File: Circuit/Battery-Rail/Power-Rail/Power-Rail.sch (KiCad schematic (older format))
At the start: 4 parts, among them P1 XT60, P2 XT60, P3 XT60, P4 XT60

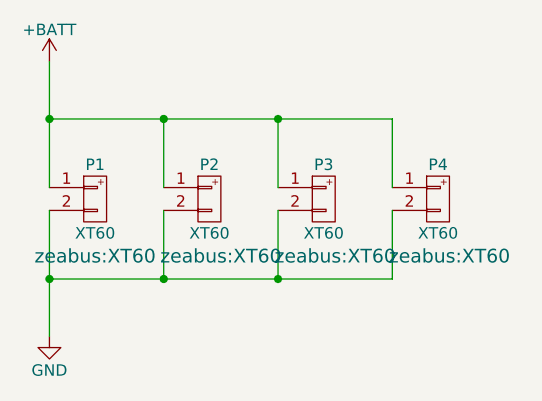
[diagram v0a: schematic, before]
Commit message: fix xt60 to close to each one on power-rail pcb
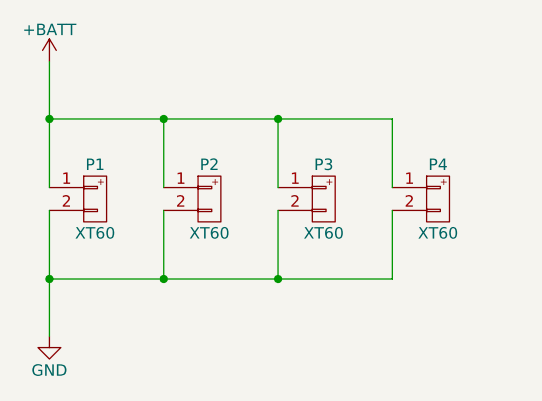
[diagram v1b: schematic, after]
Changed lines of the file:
@@
 LIBS:valves
 LIBS:zeabus
+LIBS:Power-Rail-cache
 EELAYER 25 0
 EELAYER END
@@
 Comment4 ""
 $EndDescr
-$Comp
-L XT60 P1
-U 1 1 594D2F0E
-P 5550 3850
-F 0 "P1" H 5550 4000 50  0000 C CNN
-F 1 "XT60" H 5550 3700 50  0000 C CNN
-F 2 "zeabus:XT60" H 5550 3600 60  0000 C CNN
-F 3 "" H 5550 3850 60  0000 C CNN
-	1    5550 3850
-	1    0    0    -1
-$EndComp
-$Comp
-L XT60 P2
-U 1 1 594D2F3F
-P 6050 3850
-F 0 "P2" H 6050 4000 50  0000 C CNN
-F 1 "XT60" H 6050 3700 50  0000 C CNN
-F 2 "zeabus:XT60" H 6100 3600 60  0000 C CNN
-F 3 "" H 6050 3850 60  0000 C CNN
-	1    6050 3850
-	1    0    0    -1
-$EndComp
-$Comp
-L XT60 P3
-U 1 1 594D30B5
-P 6550 3850
-F 0 "P3" H 6550 4000 50  0000 C CNN
-F 1 "XT60" H 6550 3700 50  0000 C CNN
-F 2 "zeabus:XT60" H 6600 3600 60  0000 C CNN
-F 3 "" H 6550 3850 60  0000 C CNN
-	1    6550 3850
-	1    0    0    -1
-$EndComp
-$Comp
-L XT60 P4
-U 1 1 594D30BB
-P 7050 3850
-F 0 "P4" H 7050 4000 50  0000 C CNN
-F 1 "XT60" H 7050 3700 50  0000 C CNN
-F 2 "zeabus:XT60" H 7100 3600 60  0000 C CNN
-F 3 "" H 7050 3850 60  0000 C CNN
-	1    7050 3850
-	1    0    0    -1
-$EndComp
 $Comp
 L +BATT #PWR01
@@
 	6850 4200 6850 3900
 Connection ~ 6350 4200
+$Comp
+L XT60 P1
+U 1 1 5A75305B
+P 5550 3850
+F 0 "P1" H 5550 4000 50  0000 C CNN
+F 1 "XT60" H 5550 3700 50  0000 C CNN
+F 2 "zeabus:XT60" H 5550 3850 60  0001 C CNN
+F 3 "" H 5550 3850 60  0000 C CNN
+	1    5550 3850
+	1    0    0    -1
+$EndComp
+$Comp
+L XT60 P2
+U 1 1 5A7531B6
+P 6050 3850
+F 0 "P2" H 6050 4000 50  0000 C CNN
+F 1 "XT60" H 6050 3700 50  0000 C CNN
+F 2 "zeabus:XT60" H 6050 3850 60  0001 C CNN
+F 3 "" H 6050 3850 60  0000 C CNN
+	1    6050 3850
+	1    0    0    -1
+$EndComp
+$Comp
+L XT60 P3
+U 1 1 5A7531DC
+P 6550 3850
+F 0 "P3" H 6550 4000 50  0000 C CNN
+F 1 "XT60" H 6550 3700 50  0000 C CNN
+F 2 "zeabus:XT60" H 6550 3850 60  0001 C CNN
+F 3 "" H 6550 3850 60  0000 C CNN
+	1    6550 3850
+	1    0    0    -1
+$EndComp
+$Comp
+L XT60 P4
+U 1 1 5A75320F
+P 7050 3850
+F 0 "P4" H 7050 4000 50  0000 C CNN
+F 1 "XT60" H 7050 3700 50  0000 C CNN
+F 2 "zeabus:XT60" H 7050 3850 60  0001 C CNN
+F 3 "" H 7050 3850 60  0000 C CNN
+	1    7050 3850
+	1    0    0    -1
+$EndComp
 $EndSCHEMATC
